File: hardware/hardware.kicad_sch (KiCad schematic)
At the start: 0 parts

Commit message: Schematics Completed
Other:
- sheet Connectors_Comms ports: added 3V3, 5V_CAM, RESET, SWCLK_BOOT0, SWDIO, USART2_RX, USART2_TX; removed none
- sheet Current_Sense ports: added 3V3, 5V, 5V_CAM, I2C1_SCL, I2C1_SDA; removed none
- sheet MCU ports: added 3V3, EN_RAILB, I2C1_SCL, I2C1_SDA, RESET, SWCLK_BOOT0, SWDIO, USART2_RX, USART2_TX; removed none
- sheet Power_Input_Protection ports: added 3V3, 5V, EN_RAILB, VBAT_PROT, VBAT_RAW; removed none

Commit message: Completed Schematic
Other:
- sheet Current_Sense ports: added RESET, VBAT_PROT, VBAT_RAW; removed none
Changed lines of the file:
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@@
+	)
+	(junction
+		(at 129.54 38.1)
+		(diameter 0)
+		(color 0 0 0 0)
+	)
+	(junction
+		(at 227.33 123.19)
+		(diameter 0)
+		(color 0 0 0 0)
 	)
 	(junction
@@
 	)
 	(junction
-		(at 129.54 38.1)
+		(at 81.28 34.29)
 		(diameter 0)
 		(color 0 0 0 0)
@@
 	)
 	(junction
-		(at 81.28 34.29)
+		(at 57.15 50.8)
 		(diameter 0)
 		(color 0 0 0 0)
@@
 	(wire
 		(pts
-			(xy 207.01 146.05) (xy 77.47 146.05)
+			(xy 85.09 115.57) (xy 39.37 115.57)
+		)
+		(stroke
+			(width 0)
+			(type default)
+		)
+	)
+	(wire
+		(pts
+			(xy 207.01 146.05) (xy 110.49 146.05)
+		)
+		(stroke
+			(width 0)
+			(type default)
+		)
+	)
+	(wire
+		(pts
+			(xy 39.37 115.57) (xy 39.37 50.8)
 		)
 		(stroke
@@
 	(wire
 		(pts
+			(xy 134.62 163.83) (xy 134.62 156.21)
+		)
+		(stroke
+			(width 0)
+			(type default)
+		)
+	)
+	(wire
+		(pts
 			(xy 198.12 59.69) (xy 223.52 59.69)
 		)
@@
 	(wire
 		(pts
-			(xy 77.47 102.87) (xy 129.54 102.87)
+			(xy 110.49 102.87) (xy 129.54 102.87)
 		)
 		(stroke
@@
 	(wire
 		(pts
+			(xy 102.87 38.1) (xy 120.65 38.1)
+		)
+		(stroke
+			(width 0)
+			(type default)
+		)
+	)
+	(wire
+		(pts
 			(xy 129.54 38.1) (xy 129.54 102.87)
 		)
@@
 	(wire
 		(pts
+			(xy 52.07 24.13) (xy 81.28 24.13)
+		)
+		(stroke
+			(width 0)
+			(type default)
+		)
+	)
+	(wire
+		(pts
+			(xy 227.33 123.19) (xy 231.14 123.19)
+		)
+		(stroke
+			(width 0)
+			(type default)
+		)
+	)
+	(wire
+		(pts
 			(xy 160.02 88.9) (xy 160.02 116.84)
 		)
@@
 	(wire
 		(pts
-			(xy 184.15 123.19) (xy 231.14 123.19)
+			(xy 184.15 123.19) (xy 227.33 123.19)
+		)
+		(stroke
+			(width 0)
+			(type default)
+		)
+	)
+	(wire
+		(pts
+			(xy 39.37 50.8) (xy 57.15 50.8)
 		)
 		(stroke
@@
 	(wire
 		(pts
-			(xy 102.87 38.1) (xy 120.65 38.1)
+			(xy 95.25 163.83) (xy 134.62 163.83)
 		)
 		(stroke
@@
 	(wire
 		(pts
-			(xy 124.46 109.22) (xy 77.47 109.22)
+			(xy 124.46 109.22) (xy 110.49 109.22)
+		)
+		(stroke
+			(width 0)
+			(type default)
+		)
+	)
+	(wire
+		(pts
+			(xy 81.28 34.29) (xy 81.28 24.13)
+		)
+		(stroke
+			(width 0)
+			(type default)
+		)
+	)
+	(wire
+		(pts
+			(xy 134.62 156.21) (xy 227.33 156.21)
+		)
+		(stroke
+			(width 0)
+			(type default)
+		)
+	)
+	(wire
+		(pts
+			(xy 52.07 102.87) (xy 85.09 102.87)
 		)
 		(stroke
@@
 	(wire
 		(pts
+			(xy 227.33 156.21) (xy 227.33 123.19)
+		)
+		(stroke
+			(width 0)
+			(type default)
+		)
+	)
+	(wire
+		(pts
+			(xy 171.45 38.1) (xy 171.45 40.64)
+		)
+		(stroke
+			(width 0)
+			(type default)
+		)
+	)
+	(wire
+		(pts
+			(xy 163.83 88.9) (xy 163.83 116.84)
+		)
+		(stroke
+			(width 0)
+			(type default)
+		)
+	)
+	(wire
+		(pts
+			(xy 217.17 64.77) (xy 198.12 64.77)
+		)
+		(stroke
+			(width 0)
+			(type default)
+		)
+	)
+	(wire
+		(pts
+			(xy 81.28 34.29) (xy 102.87 34.29)
+		)
+		(stroke
+			(width 0)
+			(type default)
+		)
+	)
+	(wire
+		(pts
 			(xy 120.65 38.1) (xy 129.54 38.1)
 		)
@@
 	(wire
 		(pts
-			(xy 171.45 38.1) (xy 171.45 40.64)
-		)
-		(stroke
-			(width 0)
-			(type default)
-		)
-	)
-	(wire
-		(pts
-			(xy 163.83 88.9) (xy 163.83 116.84)
-		)
-		(stroke
-			(width 0)
-			(type default)
-		)
-	)
-	(wire
-		(pts
-			(xy 217.17 64.77) (xy 198.12 64.77)
-		)
-		(stroke
-			(width 0)
-			(type default)
-		)
-	)
-	(wire
-		(pts
-			(xy 81.28 34.29) (xy 102.87 34.29)
-		)
-		(stroke
-			(width 0)
-			(type default)
-		)
-	)
-	(wire
-		(pts
 			(xy 57.15 50.8) (xy 69.85 50.8)
 		)
@@
 	(wire
 		(pts
-			(xy 77.47 127) (xy 135.89 127)
-		)
-		(stroke
-			(width 0)
-			(type default)
-		)
-	)
-	(wire
-		(pts
-			(xy 203.2 151.13) (xy 77.47 151.13)
+			(xy 95.25 157.48) (xy 95.25 163.83)
+		)
+		(stroke
+			(width 0)
+			(type default)
+		)
+	)
+	(wire
+		(pts
+			(xy 110.49 127) (xy 135.89 127)
+		)
+		(stroke
+			(width 0)
+			(type default)
+		)
+	)
+	(wire
+		(pts
+			(xy 203.2 151.13) (xy 110.49 151.13)
 		)
 		(stroke
@@
 		(pts
 			(xy 198.12 83.82) (xy 203.2 83.82)
+		)
+		(stroke
+			(width 0)
+			(type default)
+		)
+	)
+	(wire
+		(pts
+			(xy 52.07 102.87) (xy 52.07 24.13)
 		)
 		(stroke
@@
 			)
 		)
+		(pin "SWCLK_BOOT0" input
+			(at 184.15 128.27 0)
+			(effects
+				(font
+					(size 1.27 1.27)
+				)
+				(justify right)
+			)
+		)
+		(pin "SWDIO" input
+			(at 184.15 132.08 0)
+			(effects
+				(font
+					(size 1.27 1.27)
+				)
+				(justify right)
+			)
+		)
 		(pin "RESET" input
 			(at 184.15 123.19 0)
-			(effects
-				(font
-					(size 1.27 1.27)
-				)
-				(justify right)
-			)
-		)
-		(pin "SWCLK_BOOT0" input
-			(at 184.15 128.27 0)
-			(effects
-				(font
-					(size 1.27 1.27)
-				)
-				(justify right)
-			)
-		)
-		(pin "SWDIO" output
-			(at 184.15 132.08 0)
 			(effects
 				(font
@@
 	)
 	(sheet
-		(at 52.07 96.52)
+		(at 85.09 96.52)
 		(size 25.4 60.96)
 		(exclude_from_sim no)
@@
 		)
 		(property "Sheetname" "Current_Sense"
-			(at 52.07 95.8084 0)
+			(at 85.09 95.8084 0)
 			(show_name no)
 			(do_not_autoplace no)
@@
 		)
 		(property "Sheetfile" "Current_Sense.kicad_sch"
-			(at 52.07 158.0646 0)
+			(at 85.09 158.0646 0)
 			(show_name no)
 			(do_not_autoplace no)
@@
 		)
 		(pin "3V3" input
-			(at 77.47 102.87 0)
-			(effects
-				(font
-					(size 1.27 1.27)
-				)
-				(justify right)
-			)
-		)
-		(pin "5V" output
-			(at 77.47 109.22 0)
+			(at 110.49 102.87 0)
+			(effects
+				(font
+					(size 1.27 1.27)
+				)
+				(justify right)
+			)
+		)
+		(pin "5V" input
+			(at 110.49 109.22 0)
 			(effects
 				(font
@@
 		)
 		(pin "5V_CAM" output
-			(at 77.47 127 0)
+			(at 110.49 127 0)
 			(effects
 				(font
@@
 		)
 		(pin "I2C1_SCL" input
-			(at 77.47 151.13 0)
+			(at 110.49 151.13 0)
 			(effects
 				(font
@@
 		)
 		(pin "I2C1_SDA" input
-			(at 77.47 146.05 0)
-			(effects
-				(font
-					(size 1.27 1.27)
-				)
-				(justify right)
-			)
-		)
+			(at 110.49 146.05 0)
+			(effects
+				(font
+					(size 1.27 1.27)
+				)
+				(justify right)
+			)
+		)
+		(pin "RESET" input
+			(at 95.25 157.48 270)
+			(effects
+				(font
+					(size 1.27 1.27)
+				)
+				(justify left)
+			)
+		)
+		(pin "VBAT_PROT" input
+			(at 85.09 102.87 180)
+			(effects
+				(font
+					(size 1.27 1.27)
+				)
+				(justify left)
+			)
+		)
+		(pin "VBAT_RAW" input
+			(at 85.09 115.57 180)
+			(effects
+				(font
+					(size 1.27 1.27)
+				)
+				(justify left)
+			)
+		)

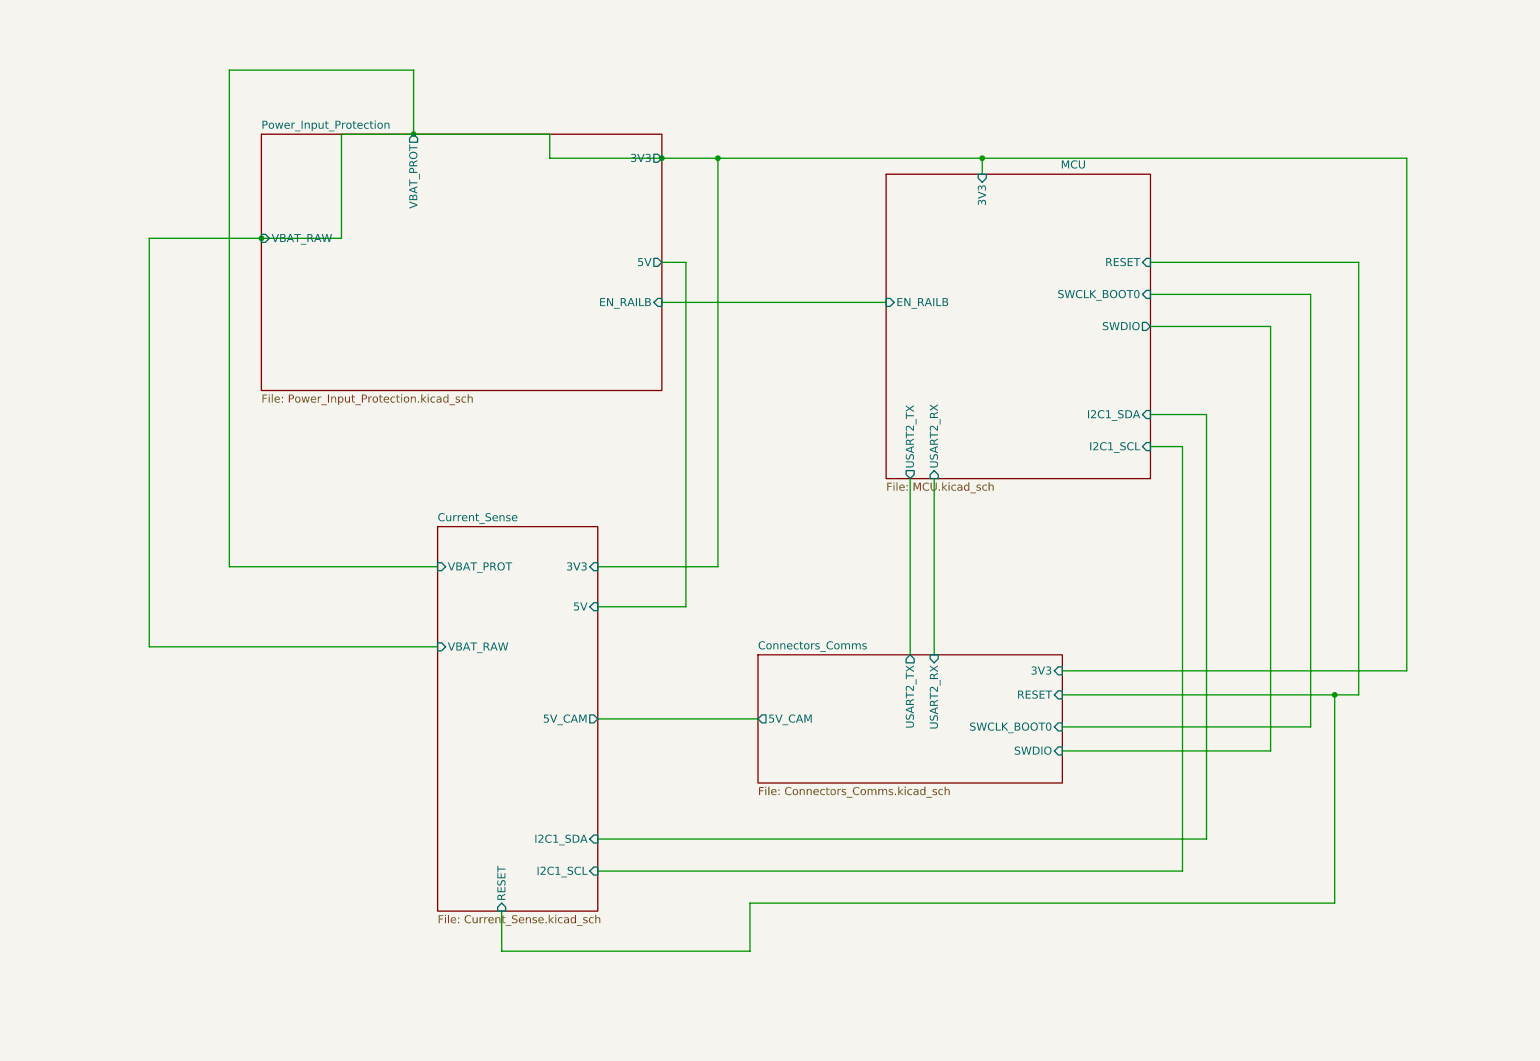
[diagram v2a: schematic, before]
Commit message: Short Circuit Fix
There were root label connections that short circuited some of the pins, so they were removed and properly addressed
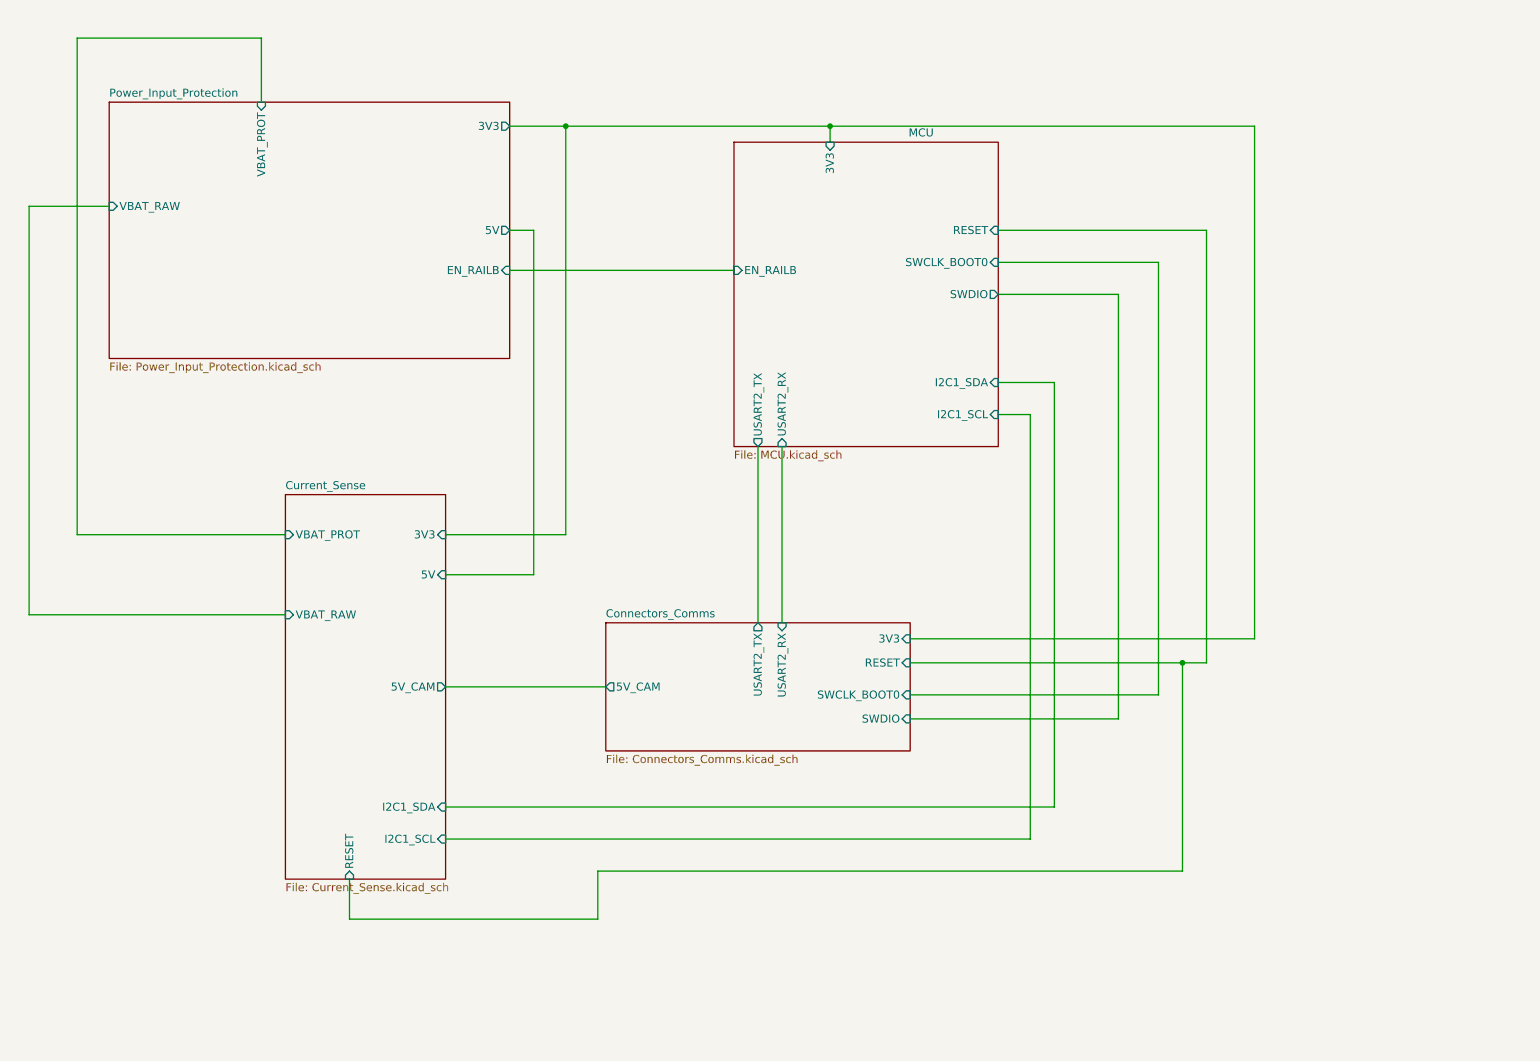
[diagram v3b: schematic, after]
